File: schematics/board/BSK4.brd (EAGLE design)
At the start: 82 x 100 mm, 33 parts

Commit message: Сделаны платы CROSSnew, SPIDERnew, BSK2
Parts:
- removed DS18B20Z: DS18B20Z, CanCubeSat:DS18B20Z
- removed FS8205A#1, FS8205A#2: FS8205A+, CanCubeSat:FS8205A+
- removed L293DD: L293DD, CanCubeSat:L293DD
- removed LAP4: LAP4-BOTTOM, led:P47F-BOTTOM
- removed LED1, LED2, LED3, LED4, LED5: (no value), led:CHIPLED_0603
- removed R1, R3, R4, R5, R81: 2k, resistor:R0603
- removed R10, R11, R2, R7: 100R, resistor:R0603
- removed R19: 1M, resistor:R0603
- removed R20: 510k, resistor:R0603
- removed U$6, U$7: EM_HEAT, CanCubeSat:EM_HEAT
- added DS18B20Z1: DS18B20Z, CanCubeSat:DS18B20Z
- added LAP1: LAP4-BOTTOM, led:P47F-BOTTOM
- added LED6, LED7: (no value), led:CHIPLED_0603
- added R12, R8: 2M, resistor:R0603
- added R13, R14: 2k, resistor:R0603
- added R15, R17, R6, R9: 1M, resistor:R0603
- added R16: 1k5, resistor:R0603
- added R94, R95: 2k26, resistor:R0603
- added U$13, U$8: SI2302CDS, CanCubeSat:SOT23-3
- added U$14: EM_HEAT, CanCubeSat:EM_HEAT
- added U$26: FS8205A+, CanCubeSat:FS8205A+
- added U$5: MOCD217M, CanCubeSat:SOIC8
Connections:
- removed net N$1: L293DD.3, LED1.C, LED2.A, U$6.1
- removed net N$10: LED3.C, R3.1
- removed net N$2: L293DD.8, R1.1, R81.1, U$6.2
- removed net N$27: LAP4.A, LED4.A, R4.2
- removed net N$28: LED5.A, R5.2
- removed net N$3: L293DD.18, LED3.A, U$7.1
- removed net N$4: FS8205A#2.4, R2.2
- removed net N$5: LED2.C, R81.2
- removed net N$6: FS8205A#2.5, R7.2
- removed net N$7: LED1.A, R1.2
- removed net N$8: FS8205A#1.4, R10.2
- removed net N$9: FS8205A#1.5, R11.2
- new net 1: R14.2, U$14.2, U$8.3
- new net 2: R16.2, U$13.3
- new net B4-KHEAT: R15.1, U$8.1
- new net B4-KVCC: R94.2, R95.2, U$5.1, U$5.3
- new net B4-ROZE: R17.1, U$13.1
- new net N$29: R6.1, R8.2, U$26.5
- new net N$30: R12.1, R9.1, U$26.4
- new net N$31: LAP1.A, R13.2
- new net N$32: LED6.C, R14.1
- new net N$33: LED7.C, R16.1
- new net N$34: DS18B20Z1.HEAT, U$26.HEAT
- new net OC1: R9.2, U$5.6
- new net OD1: R6.2, U$5.8
- net 1W: now also DS18B20Z1.4; no longer DS18B20Z.4
- net 5V: now also DS18B20Z1.3, LED6.A, R13.1, U$14.1; no longer DS18B20Z.3, L293DD.1, L293DD.10, L293DD.11, L293DD.20, R4.1, R5.1
- net B4_KEM+: no longer L293DD.2
- net B4_KEM-: no longer L293DD.9
- net B4_KHEAT: no longer L293DD.19
- net B4_KVCC: no longer R10.1, R11.1, R19.1, R20.1
- net BUS+: now also LED7.A, R12.2, R8.1; no longer R19.2
- net BUS-: now also LAP1.C, U$26.67, U$5.7; no longer FS8205A#1.23, LAP4.C, LED4.C, R20.2
- net GND: now also DS18B20Z1.5, R15.2, R17.2, R94.1, R95.1, U$13.2, U$26.23, U$5.2, U$5.4, U$5.5, U$8.2; no longer DS18B20Z.5, DS18B20Z.HEAT, FS8205A#1.67, FS8205A#1.HEAT, FS8205A#2.67, FS8205A#2.HEAT, L293DD.14, L293DD.15, L293DD.16, L293DD.17, L293DD.4, L293DD.5, L293DD.6, L293DD.7, L293DD.HEAT, R3.2, U$7.2
- net PL-: no longer FS8205A#2.23, LED5.C
- net PL_KVCC: no longer R2.1, R7.1
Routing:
- net N$27: track 111.6 -> 0.00 mm, vias 4 -> 0
- net N$2: track 76.4 -> 0.00 mm, vias 2 -> 0
- net N$1: track 69.2 -> 0.00 mm
- net N$3: track 67.3 -> 0.00 mm, vias 2 -> 0
- net GND: track 74.1 -> 31.0 mm
- net PL_KVCC: track 30.3 -> 11.0 mm, vias 3 -> 1
- net 5V: track 171.9 -> 155.1 mm, vias 7 -> 5
- net BUS-: track 110.4 -> 105.5 mm
- net B4_KVCC: track 43.9 -> 40.9 mm
- net N$9: track 2.48 -> 0.00 mm
- net PL-: track 77.4 -> 75.1 mm
- net N$28: track 2.20 -> 0.00 mm
- net N$7: track 1.94 -> 0.00 mm
- net N$5: track 1.94 -> 0.00 mm
- net N$8: track 1.78 -> 0.00 mm
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
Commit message: Плата АB+DC-DC
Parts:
- removed BSK1: (no value), pinheadCS:1X14
- removed LAP1: LAP4-BOTTOM, led:P47F-BOTTOM
- removed PAYLOAD: (no value), pinheadCS:1X08
- removed R15, R17: 1M, resistor:R0603
- removed R16: 1k5, resistor:R0603
- removed U$18, U$19, U$20, U$21: KCONNECT, CanCubeSat:KCONNECT
- added BKU: (no value), pinheadCS:1X11
- added C41: 0,1µ, rcl:C0603
- added CMD: KCONNECTQUAD, CanCubeSat:KCONNECT_QUAD
- added R1, R2: 2k26, resistor:R0603
- added R4, R7: 2k, resistor:R0603
- added R5: 100R, resistor:R0603
- added R75: R01, rcl:R2512
- added R76, R77: 10R, resistor:R0603
- added U$10, U$11, U$12, U$9: KCONNECT, CanCubeSat:KCONNECT
- added U$15, U$16, U$6, U$7: GRAFITGRAFIT3_1, CanCubeSat:GRAFIT3_1
- added U$57: INA219AID, CanCubeSat:SOT23-8
- added YELLOW: LAP4-BOTTOM, led:P47F-BOTTOM
- DS18B20Z1: device CanCubeSat:DS18B20Z -> CanCubeSat:SOIC8+HEAT_S
- R12: value 2M -> 100k
- R13: value 2k -> 1k5
- R14: value 2k -> 1M
- R6: value 1M -> 100k
- R8: value 2M -> 1M
- R9: value 1M -> 100R
- R94, R95: value 2k26 -> 200k
- moved R6 124.3 mm to (27.0, 89.7), turned to 270 degrees
- moved R9 123.8 mm to (31.6, 89.7), turned to 90 degrees
- moved R12 120.8 mm to (29.3, 89.7), turned to 90 degrees
- moved R95 106.3 mm to (38.6, 82.0)
- moved R94 105.1 mm to (38.6, 79.6)
- moved U$26 103.1 mm to (28.3, 86.4), turned to 90 degrees
- moved U$5 102.8 mm to (39.6, 87.9)
- moved R13 101.1 mm to (66.5, 53.2)
- moved LED7 99.7 mm to (66.4, 55.6), turned to 90 degrees
- moved R14 93.0 mm to (66.5, 46.6)
- moved LED6 92.0 mm to (9.70, 68.1)
- moved U$8 91.8 mm to (7.80, 59.2)
- moved U$13 90.8 mm to (66.5, 49.4)
- moved R8 89.2 mm to (7.80, 56.4)
- moved DS18B20Z1 87.9 mm to (31.8, 80.2), turned to 270 degrees
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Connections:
- net BUS+1 renamed SP+1
- net BUS-1 renamed SP-1
- removed net B4_KEM+: BSK1.11
- removed net B4_KEM-: BSK1.10
- removed net B4_KHEAT: BSK1.12
- removed net B4_KVCC: BSK1.13
- removed net BUS+2: U$18.1, U$18.2, U$18.3, U$18.4, U$18.P$1, U$18.P$2
- removed net BUS+3: U$20.1, U$20.2, U$20.3, U$20.4, U$20.P$1, U$20.P$2
- removed net BUS-: LAP1.C, U$2.1, U$2.2, U$2.3, U$2.4, U$2.P$1, U$2.P$2, U$26.67, U$5.7
- removed net BUS-2: U$19.1, U$19.2, U$19.3, U$19.4, U$19.P$1, U$19.P$2
- removed net BUS-3: U$21.1, U$21.2, U$21.3, U$21.4, U$21.P$1, U$21.P$2
- removed net I2CINT: BSK1.5, PAYLOAD.6
- removed net N$32: LED6.C, R14.1
- removed net N$33: LED7.C, R16.1
- removed net N$34: DS18B20Z1.HEAT, U$26.HEAT
- removed net PL-: PAYLOAD.1
- removed net PL_KVCC: BSK1.8
- removed net SCLTM: BSK1.7, PAYLOAD.8
- removed net SDATM: BSK1.6, PAYLOAD.7
- removed net TIME: BSK1.4, PAYLOAD.5
- removed net VDD: BSK1.1, PAYLOAD.2
- new net 3V3: BKU.8, U$57.4, U$57.8
- new net B4-CMD: BKU.4, CMD.1, CMD.2, CMD.3, CMD.4, CMD.P$1, CMD.P$2
- new net N$150: C41.1, R76.2, U$57.1
- new net N$151: C41.2, R77.2, U$57.2
- new net N$17: R1.1, R94.2, U$5.1
- new net N$18: R2.1, R95.2, U$5.3
- new net N$26: R5.1, R6.2, U$26.5
- new net N$28: R4.2, YELLOW.A
- new net SCL-INA: BKU.10, U$57.5
- new net SDA-INA: BKU.11, U$57.6
- new net SP+: R75.1, R77.1, U$3.1, U$3.2, U$3.3, U$3.4, U$3.P$1, U$3.P$2
- new net SP+2: U$9.1, U$9.2, U$9.3, U$9.4, U$9.P$1, U$9.P$2
- new net SP+3: U$11.1, U$11.2, U$11.3, U$11.4, U$11.P$1, U$11.P$2
- new net SP-: U$2.1, U$2.2, U$2.3, U$2.4, U$2.P$1, U$2.P$2, U$26.67, U$5.7, YELLOW.C
- new net SP-2: U$10.1, U$10.2, U$10.3, U$10.4, U$10.P$1, U$10.P$2
- new net SP-3: U$12.1, U$12.2, U$12.3, U$12.4, U$12.P$1, U$12.P$2
- net 1: now also R7.2; no longer R14.2
- net 1W: now also BKU.5; no longer BSK1.14
- net 2: now also R13.2, U$15.P$1, U$16.P$1, U$6.P$1, U$7.P$1; no longer R16.2
- net 5V: now also BKU.7, R4.1; no longer BSK1.2, PAYLOAD.3, R13.1
- net B4-KHEAT: now also BKU.1, R8.1; no longer R15.1
- net B4-KVCC: now also BKU.2, R1.2, R2.2; no longer R94.2, R95.2, U$5.1, U$5.3
- net B4-ROZE: now also BKU.3, R14.1; no longer R17.1
- net BUS+: now also BKU.6, R6.1, R75.2, R76.1, U$15.P$2, U$16.P$2, U$6.P$2, U$7.P$2; no longer BSK1.3, PAYLOAD.4, R8.1, U$3.1, U$3.2, U$3.3, U$3.4, U$3.P$1, U$3.P$2
- net GND: now also BKU.9, DS18B20Z1.HEAT, R14.2, R8.2, U$26.HEAT, U$57.3, U$57.7; no longer BSK1.9, R15.2, R17.2
- net N$29: now also LED7.C, R13.1; no longer R6.1, R8.2, U$26.5
- net N$31: now also LED6.C, R7.1; no longer LAP1.A, R13.2
- net OD1: now also R5.2; no longer R6.2
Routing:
- net TIME: track 135.0 -> 0.00 mm, vias 1 -> 0
- net I2CINT: track 128.4 -> 0.00 mm, vias 1 -> 0
- net 2: track 0.00 -> 126.5 mm, vias 0 -> 5
- net SP-: track 0.00 -> 125.7 mm, vias 0 -> 2
- net VDD: track 112.5 -> 0.00 mm
- net SDATM: track 111.7 -> 0.00 mm, vias 1 -> 0
- net SCLTM: track 109.4 -> 0.00 mm, vias 1 -> 0
- net BUS-: track 105.5 -> 0.00 mm, vias 3 -> 0
- net BUS+: track 123.0 -> 217.7 mm, vias 1 -> 2
- net B4-ROZE: track 0.00 -> 76.4 mm, vias 0 -> 2
- net PL-: track 75.1 -> 0.00 mm, vias 1 -> 0
- net B4-CMD: track 0.00 -> 73.6 mm, vias 0 -> 3
- net B4-KHEAT: track 0.00 -> 48.4 mm, vias 0 -> 1
- net B4_KVCC: track 40.9 -> 0.00 mm, vias 2 -> 0
- net 5V: track 155.1 -> 118.7 mm, vias 5 -> 6
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- added copper zone on layer 1, net GND1
- added copper zone on layer 1, net GND2
- added copper zone on layer 1, net GND3
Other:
- outline, holes or cut-outs redrawn
- board text added: "BSK2 "Концерн ИТС""
- board text added: "to BKU"
- board text removed: "BSK4 "Концерн ИТС""
- board text removed: "BUS"
- board text removed: "EM+"
- board text removed: "EM-"
- board text removed: "PL"
- board text removed: "to BSK1"
- board text removed: "to PAYLOAD"

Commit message: Изменен номинал резисторов
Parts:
- R13: value 1k5 -> 3k3
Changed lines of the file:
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@@
 </element>
 <element name="U$13" library="CanCubeSat" package="SOT23-3" value="SI2302CDS" x="66.5" y="49.4" smashed="yes"/>
-<element name="R13" library="resistor" library_urn="urn:adsk.eagle:library:348" package="R0603" package3d_urn="urn:adsk.eagle:package:23555/3" value="1k5" x="66.5" y="53.2" smashed="yes">
+<element name="R13" library="resistor" library_urn="urn:adsk.eagle:library:348" package="R0603" package3d_urn="urn:adsk.eagle:package:23555/3" value="3k3" x="66.5" y="53.2" smashed="yes">
 <attribute name="VALUE" x="65.865" y="51.295" size="1.27" layer="27"/>
 </element>

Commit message: Внесены правки в платы БСК
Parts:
- added R3, R32: 100R, resistor:R0603
- moved LED7 2.00 mm to (68.4, 55.6)
- moved R13 2.00 mm to (68.5, 53.2)
- moved R14 2.00 mm to (68.5, 46.6)
- moved U$13 2.00 mm to (68.5, 49.4)
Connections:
- new net N$19: R32.1, R8.1, U$8.1
- new net N$20: R14.1, R3.1, U$13.1
- net B4-KHEAT: now also R32.2; no longer R8.1, U$8.1
- net B4-ROZE: now also R3.2; no longer R14.1, U$13.1
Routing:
- net N$19: track 0.00 -> 4.04 mm
- net BUS+: track 217.7 -> 221.7 mm
- net N$20: track 0.00 -> 3.94 mm
- net 2: track 126.5 -> 128.5 mm
- net B4-KHEAT: track 48.4 -> 47.0 mm
- net B4-ROZE: track 76.4 -> 75.6 mm

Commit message: Две линии i2c на платах БСК заменены на одну
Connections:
- net SCL-INA renamed SCL-TM
- net SDA-INA renamed SDA-TM
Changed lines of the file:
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@@
 <via x="73.9" y="98.9" extent="1-16" drill="1"/>
 </signal>
-<signal name="SCL-INA">
+<signal name="SCL-TM">
 <contactref element="U$57" pad="5"/>
 <contactref element="BKU" pad="10"/>
@@
 <wire x1="59.075" y1="91.2493" x2="59.075" y2="89.7" width="0.3" layer="1"/>
 </signal>
-<signal name="SDA-INA">
+<signal name="SDA-TM">
 <contactref element="U$57" pad="6"/>
 <contactref element="BKU" pad="11"/>

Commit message: Добавлена схема дозиметра, исправлены платы СБ
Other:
- outline, holes or cut-outs redrawn
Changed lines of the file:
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@@
 <wire x1="82" y1="8.5" x2="75" y2="8.5" width="0.1524" layer="20"/>
 <wire x1="75" y1="8.5" x2="75" y2="0" width="0.1524" layer="20"/>
-<wire x1="75" y1="0" x2="7" y2="0" width="0.1524" layer="20"/>
 <wire x1="7" y1="0" x2="7" y2="8.5" width="0.1524" layer="20"/>
 <wire x1="7" y1="8.5" x2="0" y2="8.5" width="0.1524" layer="20"/>
@@
 <text x="31.6" y="96.1" size="2" layer="26" rot="MR0" align="top-right">to BKU</text>
 <text x="5.4" y="45.6" size="1.778" layer="21" rot="R90" align="bottom-center">HEATER</text>
+<wire x1="62.96" y1="0" x2="61.67" y2="3.53" width="0.1524" layer="20"/>
+<wire x1="61.67" y1="3.53" x2="61" y2="4" width="0.1524" layer="20" curve="69.947894"/>
+<wire x1="61" y1="4" x2="51" y2="4" width="0.1524" layer="20"/>
+<wire x1="51" y1="4" x2="50.33" y2="3.53" width="0.1524" layer="20" curve="69.947894"/>
+<wire x1="50.33" y1="3.53" x2="49.04" y2="0" width="0.1524" layer="20"/>
+<wire x1="7" y1="0" x2="49.04" y2="0" width="0.1524" layer="20"/>
+<wire x1="75" y1="0" x2="62.96" y2="0" width="0.1524" layer="20"/>
 </plain>
 <attributes>

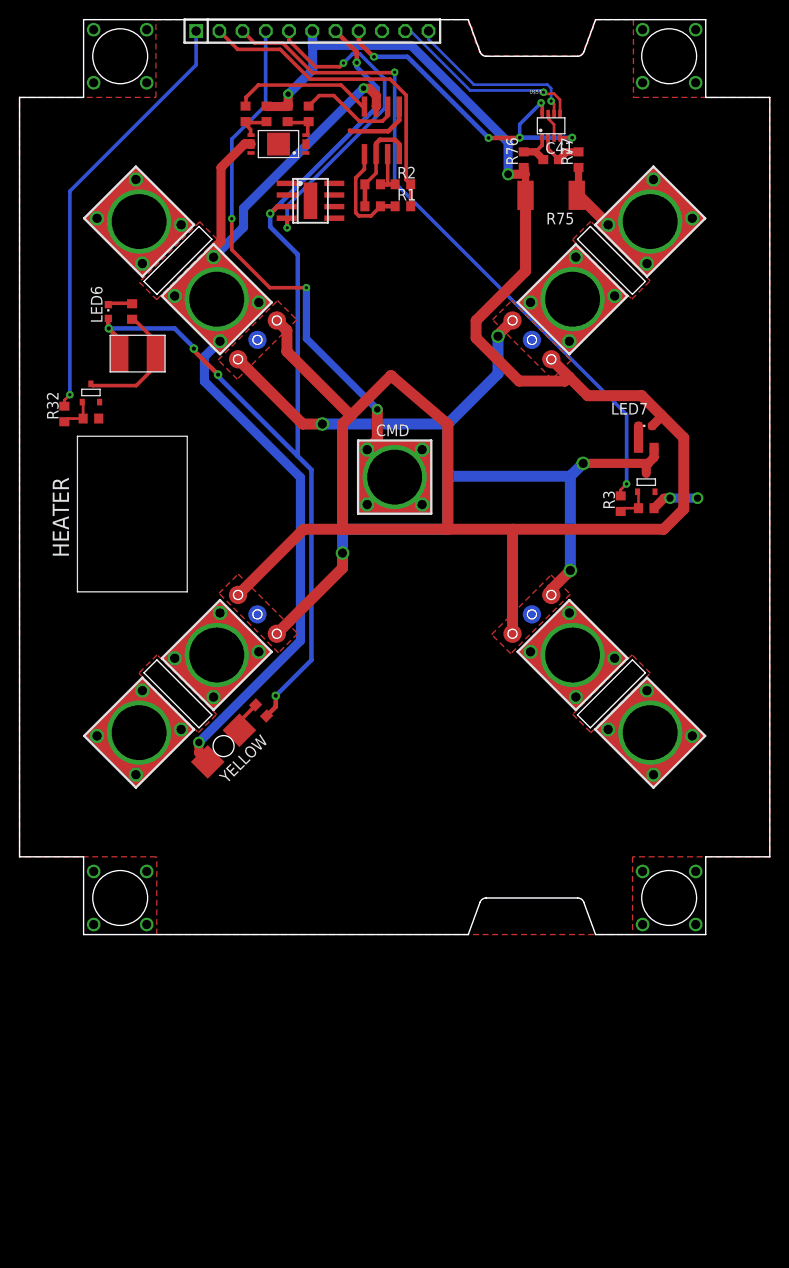
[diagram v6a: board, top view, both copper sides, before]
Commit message: Обновлен список плат, работа над платой ПН
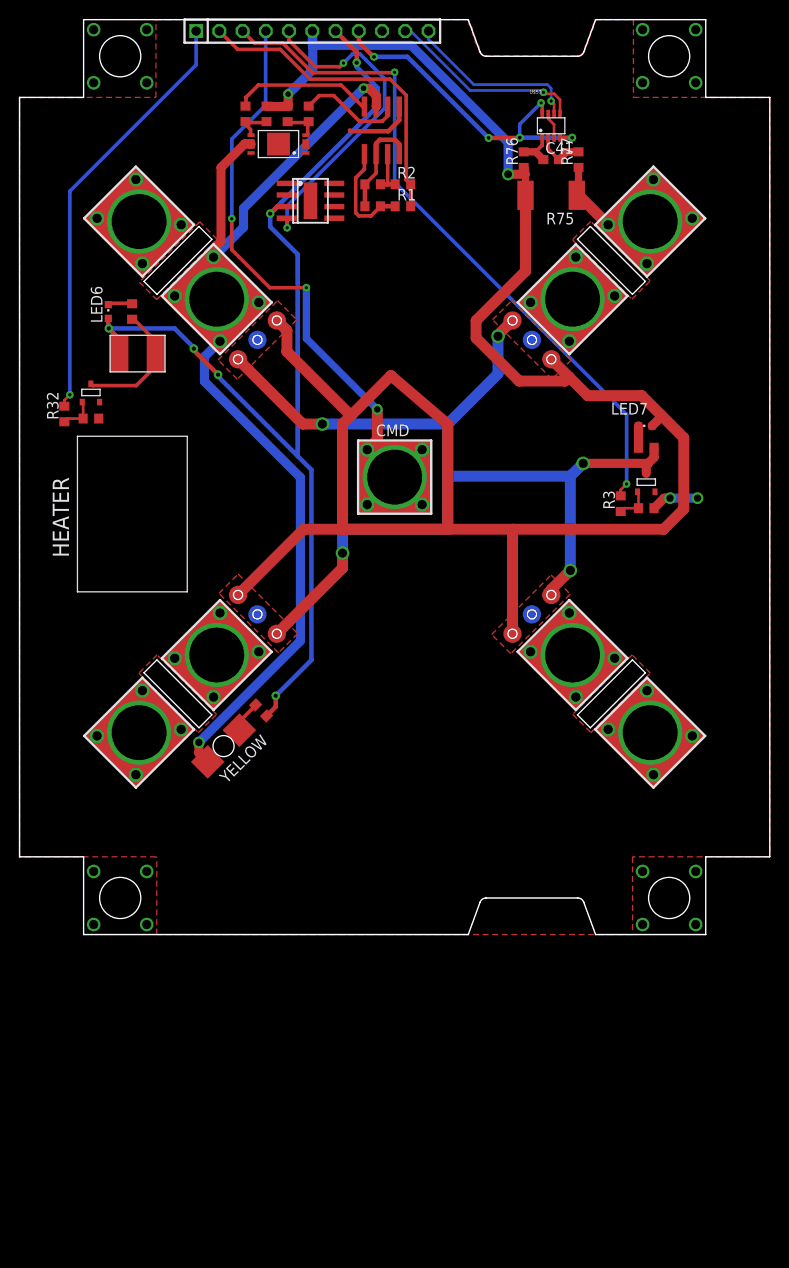
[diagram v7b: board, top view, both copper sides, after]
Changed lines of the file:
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@@
 <wire x1="7" y1="0" x2="7" y2="8.5" width="0.1524" layer="20"/>
 <wire x1="7" y1="8.5" x2="0" y2="8.5" width="0.1524" layer="20"/>
-<hole x="11" y="4" drill="6"/>
+<hole x="11" y="4" drill="4.5"/>
 <wire x1="60.976" y1="24.014" x2="66.986" y2="30.024" width="0.05" layer="20"/>
 <wire x1="66.986" y1="30.024" x2="68.4" y2="28.61" width="0.05" layer="20"/>
@@
 <wire x1="15.014" y1="30.024" x2="21.024" y2="24.014" width="0.05" layer="20"/>
 <wire x1="21.024" y1="24.014" x2="19.61" y2="22.6" width="0.05" layer="20"/>
-<hole x="71" y="4" drill="6"/>
-<hole x="71" y="96" drill="6"/>
-<hole x="11" y="96" drill="6"/>
+<hole x="71" y="4" drill="4.5"/>
+<hole x="71" y="96" drill="4.5"/>
+<hole x="11" y="96" drill="4.5"/>
 <wire x1="49.04" y1="100" x2="50.33" y2="96.47" width="0.1524" layer="20"/>
 <wire x1="50.33" y1="96.47" x2="51" y2="96" width="0.1524" layer="20" curve="69.947894"/>

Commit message: Схема БКУ
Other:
- outline, holes or cut-outs redrawn
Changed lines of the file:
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@@
 <text x="31.6" y="96.1" size="2" layer="26" rot="MR0" align="top-right">to BKU</text>
 <text x="5.4" y="45.6" size="1.778" layer="21" rot="R90" align="bottom-center">HEATER</text>
-<wire x1="62.96" y1="0" x2="61.67" y2="3.53" width="0.1524" layer="20"/>
-<wire x1="61.67" y1="3.53" x2="61" y2="4" width="0.1524" layer="20" curve="69.947894"/>
-<wire x1="61" y1="4" x2="51" y2="4" width="0.1524" layer="20"/>
-<wire x1="51" y1="4" x2="50.33" y2="3.53" width="0.1524" layer="20" curve="69.947894"/>
-<wire x1="50.33" y1="3.53" x2="49.04" y2="0" width="0.1524" layer="20"/>
-<wire x1="7" y1="0" x2="49.04" y2="0" width="0.1524" layer="20"/>
-<wire x1="75" y1="0" x2="62.96" y2="0" width="0.1524" layer="20"/>
+<wire x1="7" y1="0" x2="49" y2="0" width="0.1524" layer="20"/>
+<wire x1="75" y1="0" x2="63" y2="0" width="0.1524" layer="20"/>
+<wire x1="49" y1="0" x2="63" y2="0" width="0.1524" layer="20"/>
 </plain>
 <attributes>
